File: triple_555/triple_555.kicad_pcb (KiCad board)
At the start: 2 copper layers, 47 x 41 mm, 24 parts, among them J1 Conn_01x04, J2 Conn_01x04, U1 NA555P, U2 NA555P, U3 NA555P

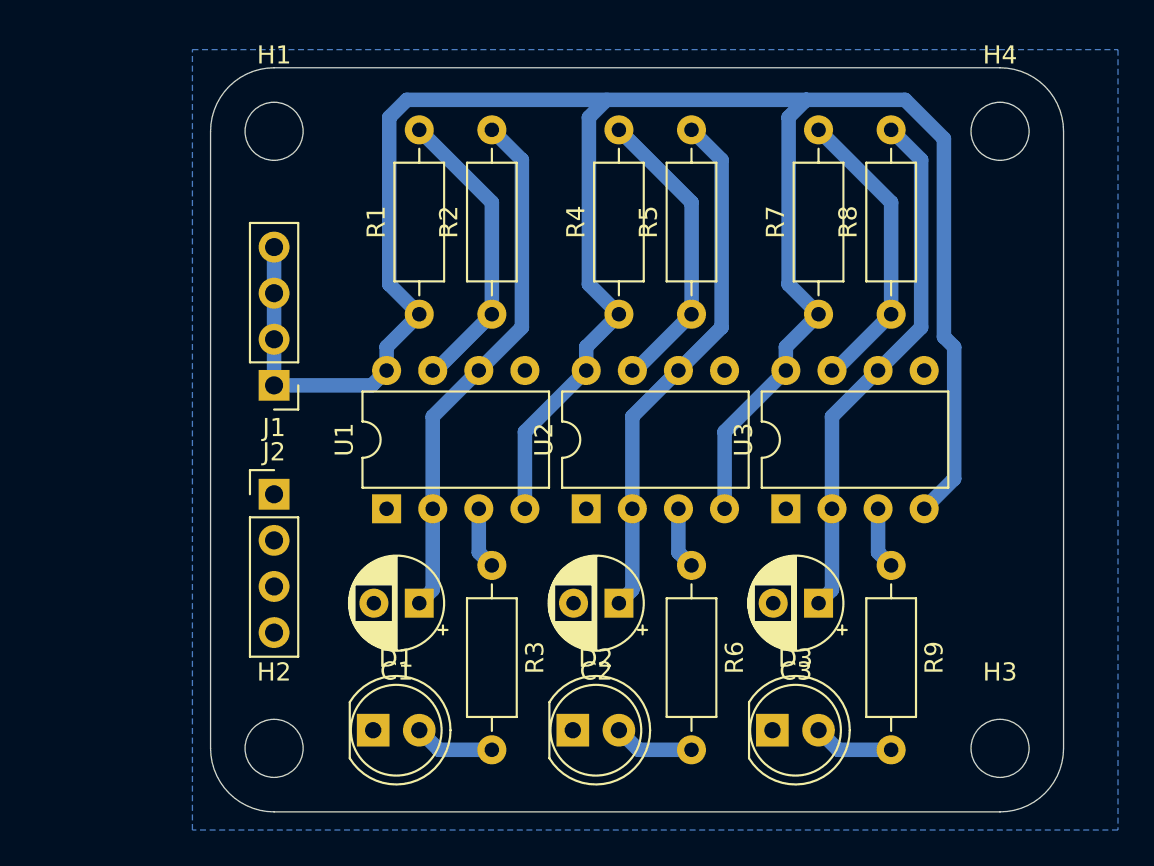
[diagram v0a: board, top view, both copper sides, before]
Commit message: add usb b connector
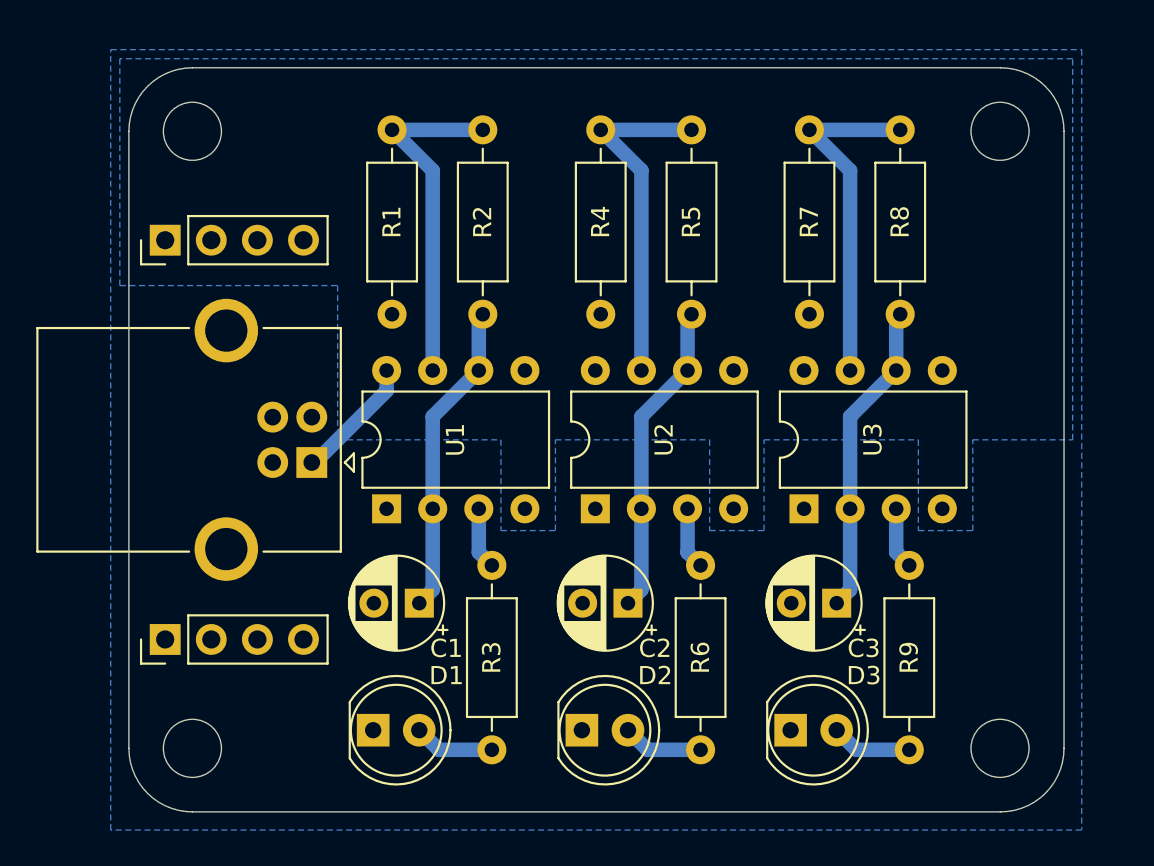
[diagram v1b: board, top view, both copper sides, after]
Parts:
- added J3: USB_B, pl_usb:USB_B_mill_spacing, F.Cu at (130.1, 101.2)
- moved R2 10.2 mm to (139.5, 82.9), turned to -90 degrees
- moved R8 10.2 mm to (162.5, 82.9), turned to -90 degrees
- moved R5 10.2 mm to (151.0, 82.9), turned to -90 degrees
- moved J1 10.0 mm to (122.0, 89.0), turned to 90 degrees
- moved J2 10.0 mm to (122.0, 111.0), turned to 90 degrees
- moved H1 4.50 mm to (123.5, 83.0)
- moved H2 4.50 mm to (123.5, 117.0)
- moved R1 1.50 mm to (134.5, 93.1)
- moved C3 1.00 mm to (159.0, 109.0)
- moved D3 1.00 mm to (156.5, 116.0)
- moved R4 1.00 mm to (146.0, 93.1)
- moved R9 1.00 mm to (163.0, 106.9)
- moved U3 1.00 mm to (157.2, 103.8)
- moved C2 0.50 mm to (147.5, 109.0)
- moved D2 0.50 mm to (145.0, 116.0)
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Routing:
- net VCC: track 134.2 -> 6.88 mm
- net Net-(U3-THR): track 29.1 -> 17.4 mm
- net Net-(U1-THR): track 29.1 -> 17.4 mm
- net Net-(U2-THR): track 29.1 -> 17.4 mm
- net Net-(U3-DIS): track 16.4 -> 19.2 mm
- net Net-(U2-DIS): track 16.4 -> 19.2 mm
- net Net-(U1-DIS): track 16.4 -> 19.2 mm
- added copper zone on B.Cu, net VCC
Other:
- board size 47 x 41 mm -> 51.5 x 41 mm
